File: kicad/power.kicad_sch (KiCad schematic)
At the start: 23 parts, among them Q1 AO3407A, Q4 AO3407A, SW2 SS-12F49-G050, U4 MP2322GQH-Z

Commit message: Updates to power
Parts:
- removed C46: 47uF, MyParts:C1206, symbol MyParts:GRM31CR61E476ME44L
- removed C47: 100nF, MyParts:C0603, symbol MyParts:CC0603KRX7R9BB104
- removed C48: 100nF, PCM_JLCPCB:C_0402, symbol PCM_JLCPCB-Capacitors:0402,100nF,(2)
- removed C49, C50: 10uF, PCM_JLCPCB:C_0805, symbol PCM_JLCPCB-Capacitors:0805,10uF,(2)
- removed C51: 100nF, PCM_JLCPCB:C_0603, symbol PCM_JLCPCB-Capacitors:0603,100nF
- removed C52: 22pF, PCM_JLCPCB:C_0603, symbol PCM_JLCPCB-Capacitors:0603,22pF
- removed C53: 22uF, PCM_JLCPCB:C_0805, symbol PCM_JLCPCB-Capacitors:0805,22uF
- removed C54: 1uF, PCM_JLCPCB:C_0402, symbol PCM_JLCPCB-Capacitors:0402,1uF
- removed DC1: DC-005-2.5A-2.0, MyParts:CONN-TH_DC-005-2.5A-2.0, symbol MyParts:DC-005-2.5A-2.0
- removed F1: 1812L110/48QR, MyParts:F1812, symbol MyParts:1812L110_48QR
- removed L11: 3.3uH, MyParts:IND-SMD_L3.0-W3.0-1, symbol MyParts:ANR3015T4R7M
- removed Q1, Q4: AO3407A, MyParts:SOT-23-3_L2.9-W1.6-P1.90-LS2.8-BR, symbol MyParts:AO3407A
- removed R20: 10kΩ, PCM_JLCPCB:R_0603, symbol PCM_JLCPCB-Resistors:0603,10kΩ
- removed R21: 976kΩ, Resistor_SMD:R_0805_2012Metric, symbol Device:R
- removed R22: 100kΩ, PCM_JLCPCB:R_0603, symbol PCM_JLCPCB-Resistors:0603,100kΩ
- removed R23: 220kΩ, PCM_JLCPCB:R_0603, symbol PCM_JLCPCB-Resistors:0603,220kΩ
- removed SW2: SS-12F49-G050, MyParts:SW-TH_SS-12F45-GXXX, symbol MyParts:SS-12F49-G050
- removed TP3: RH-5016, MyParts:TESTPOINT-SMD_L3.0-W2.0, symbol MyParts:RH-5016
- removed U4: MP2322GQH-Z, MyParts:QFN-8_L2.0-W1.5-P0.50-BL, symbol MyParts:MP2322GQH-Z
- added DC1: DC007B-2.5-J, MyParts:DC-IN-TH_HX-DC007B-2.5, symbol MyParts:DC007B-2.5-J
- added Q11, Q12: DMP3013SFV-7, MyParts:DFN-8_L3.3-W3.3-P0.65-BL, symbol MyParts:DMP3013SFV-7
- added R21: 10kΩ, PCM_JLCPCB:R_0603, symbol PCM_JLCPCB-Resistors:0603,10kΩ
- added SW4: SS-12F49-G050, MyParts:SW-TH_SS-12F45-GXXX, symbol MyParts:SS-12F49-G050
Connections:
- net 12V: now also Q12.5 (D)
- net 12V_IN: now also DC1.1, Q11.5 (D)
- net GND: now also DC1.2, DC1.3, Q11.4 (G), SW4.3
- new net: Q11.1 (S), Q11.2 (S), Q11.3 (S), Q12.1 (S), Q12.2 (S), Q12.3 (S), R21.1
- new net: R21.2, SW4.1
- new net: Q12.4 (G), SW4.2
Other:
- added sheet Power_3V3 (power_3v3.kicad_sch)
- added sheet Power_5V (power_5v.kicad_sch)
- note added: "12V DC input jack"
- note added: "12V in Out 5V and 3V3"
- note added: "2.5mm 20V 6.8mm 7A DC Power Jack Right Angle"
- note removed: "->"
- note removed: "0.1%"
- note removed: "1%"
- note removed: "1.1A Fuse 48VDC"
- note removed: "12V DC input fused to 1.1A max"
- note removed: "12V to 3V3 Buck"
- note removed: "12V_IN_FUSED is the input, 12V is the output (load)"
- note removed: "25V"
- note removed: "50V"
- note removed: "Circuit to convert 12V DC to 3V3 DC 12V is reverse polatiry and over voltage protected MP2322 used to convert 12V to 3V3 DC 12V DC out will draw max 600mA 3V3 DC out will draw max 400mA Buck modeled after John Teel's YouTube video: https://www.youtube.com/watch?v=rLHW4gU6idU and referencing the MP2322 datasheet"
- note removed: "From MP2322 Datasheet:"
- note removed: "Notes:"
- note removed: "Off"
- note removed: "On"
- note removed: "Q4 protects against reverse polarity. SW2 controls the gate of Q1, turning current on/off. The MOSFET is P-Channel."
- note removed: "gate"
- moved on the sheet: TP1

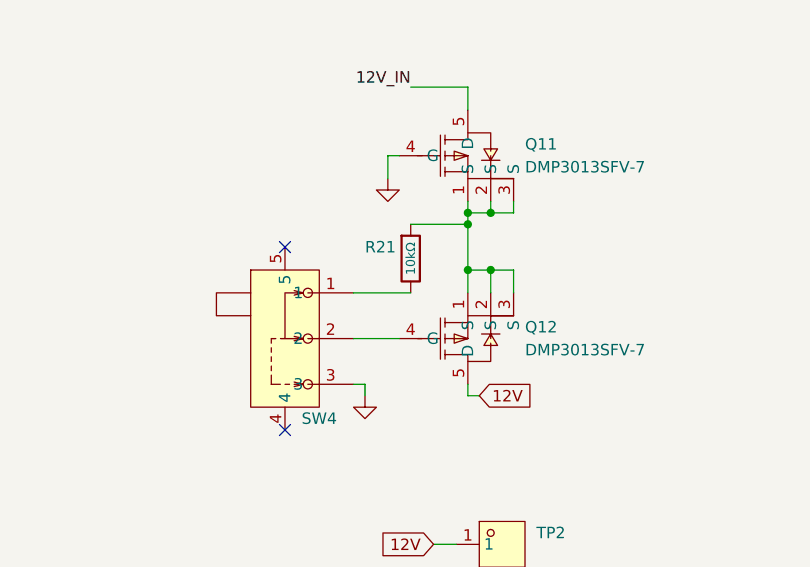
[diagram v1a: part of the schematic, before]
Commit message: Working on CM4 IO
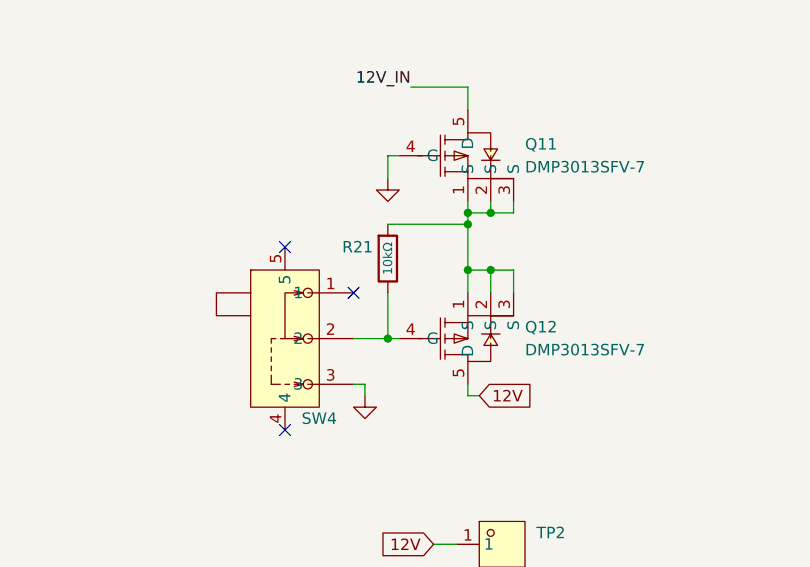
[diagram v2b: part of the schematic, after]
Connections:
- net at R21.2: now also Q12.4 (G), SW4.2; no longer SW4.1
- no-connect marks 2 -> 3
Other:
- moved on the sheet: R21
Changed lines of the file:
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@@
+	)
+	(junction
+		(at 161.29 49.53)
+		(diameter 0)
+		(color 0 0 0 0)
 	)
 	(junction
@@
 	)
 	(no_connect
+		(at 157.48 44.45)
+	)
+	(no_connect
 		(at 149.86 39.37)
 	)
@@
 	(wire
 		(pts
-			(xy 163.83 36.83) (xy 170.18 36.83)
-		)
-		(stroke
-			(width 0)
-			(type default)
-		)
-	)
-	(wire
-		(pts
 			(xy 170.18 24.13) (xy 170.18 21.59)
 		)
@@
 	(wire
 		(pts
+			(xy 161.29 44.45) (xy 161.29 49.53)
+		)
+		(stroke
+			(width 0)
+			(type default)
+		)
+	)
+	(wire
+		(pts
 			(xy 170.18 55.88) (xy 171.45 55.88)
 		)
@@
 	(wire
 		(pts
+			(xy 161.29 36.83) (xy 170.18 36.83)
+		)
+		(stroke
+			(width 0)
+			(type default)
+		)
+	)
+	(wire
+		(pts
 			(xy 170.18 41.91) (xy 170.18 44.45)
 		)
@@
 		(pts
 			(xy 91.44 41.91) (xy 92.71 41.91)
-		)
-		(stroke
-			(width 0)
-			(type default)
-		)
-	)
-	(wire
-		(pts
-			(xy 157.48 44.45) (xy 163.83 44.45)
 		)
 		(stroke
@@
 	(symbol
 		(lib_id "PCM_JLCPCB-Resistors:0603,10kΩ")
-		(at 163.83 40.64 0)
+		(at 161.29 40.64 0)
 		(unit 1)
 		(body_style 1)
@@
 		(dnp no)
 		(property "Reference" "R21"
-			(at 158.75 39.37 0)
+			(at 156.21 39.37 0)
 			(show_name no)
 			(do_not_autoplace no)
@@
 		)
 		(property "Value" "10kΩ"
-			(at 163.83 40.64 90)
+			(at 161.29 40.64 90)
 			(show_name no)
 			(do_not_autoplace yes)
@@
 		)
 		(property "Footprint" "PCM_JLCPCB:R_0603"
-			(at 162.052 40.64 90)
+			(at 159.512 40.64 90)
 			(hide yes)
 			(show_name no)
@@
 		)
 		(property "Datasheet" "https://www.lcsc.com/datasheet/lcsc_datasheet_2206010045_UNI-ROYAL-Uniroyal-Elec-0603WAF1002T5E_C25804.pdf"
-			(at 163.83 40.64 0)
+			(at 161.29 40.64 0)
 			(hide yes)
 			(show_name no)
@@
 		)
 		(property "Description" "100mW Thick Film Resistors 75V ±100ppm/°C ±1% 10kΩ 0603 Chip Resistor - Surface Mount ROHS"
-			(at 163.83 40.64 0)
+			(at 161.29 40.64 0)
 			(hide yes)
 			(show_name no)
@@
 		)
 		(property "LCSC" "C25804"
-			(at 163.83 40.64 0)
+			(at 161.29 40.64 0)
 			(hide yes)
 			(show_name no)
@@
 		)
 		(property "Stock" "51181774"
-			(at 163.83 40.64 0)
+			(at 161.29 40.64 0)
 			(hide yes)
 			(show_name no)
@@
 		)
 		(property "Price" "0.004USD"
-			(at 163.83 40.64 0)
+			(at 161.29 40.64 0)
 			(hide yes)
 			(show_name no)
@@
 		)
 		(property "Process" "SMT"
-			(at 163.83 40.64 0)
+			(at 161.29 40.64 0)
 			(hide yes)
 			(show_name no)
@@
 		)
 		(property "Minimum Qty" "20"
-			(at 163.83 40.64 0)
+			(at 161.29 40.64 0)
 			(hide yes)
 			(show_name no)
@@
 		)
 		(property "Attrition Qty" "10"
-			(at 163.83 40.64 0)
+			(at 161.29 40.64 0)
 			(hide yes)
 			(show_name no)
@@
 		)
 		(property "Class" "Basic Component"
-			(at 163.83 40.64 0)
+			(at 161.29 40.64 0)
 			(hide yes)
 			(show_name no)
@@
 		)
 		(property "Category" "Resistors,Chip Resistor - Surface Mount"
-			(at 163.83 40.64 0)
+			(at 161.29 40.64 0)
 			(hide yes)
 			(show_name no)
@@
 		)
 		(property "Manufacturer" "UNI-ROYAL(Uniroyal Elec)"
-			(at 163.83 40.64 0)
+			(at 161.29 40.64 0)
 			(hide yes)
 			(show_name no)
@@
 		)
 		(property "Part" "0603WAF1002T5E"
-			(at 163.83 40.64 0)
+			(at 161.29 40.64 0)
 			(hide yes)
 			(show_name no)
@@
 		)
 		(property "Resistance" "10kΩ"
-			(at 163.83 40.64 0)
+			(at 161.29 40.64 0)
 			(hide yes)
 			(show_name no)
@@
 		)
 		(property "Power(Watts)" "100mW"
-			(at 163.83 40.64 0)
+			(at 161.29 40.64 0)
 			(hide yes)
 			(show_name no)
@@
 		)
 		(property "Type" "Thick Film Resistors"
-			(at 163.83 40.64 0)
+			(at 161.29 40.64 0)
 			(hide yes)
 			(show_name no)
@@
 		)
 		(property "Overload Voltage (Max)" "75V"
-			(at 163.83 40.64 0)
+			(at 161.29 40.64 0)
 			(hide yes)
 			(show_name no)
@@
 		)
 		(property "Operating Temperature Range" "-55°C~+155°C"
-			(at 163.83 40.64 0)
+			(at 161.29 40.64 0)
 			(hide yes)
 			(show_name no)
@@
 		)
 		(property "Tolerance" "±1%"
-			(at 163.83 40.64 0)
+			(at 161.29 40.64 0)
 			(hide yes)
 			(show_name no)
@@
 		)
 		(property "Temperature Coefficient" "±100ppm/°C"
-			(at 163.83 40.64 0)
-			(hide yes)
-			(show_name no)
+			(at 161.29 40.64 0)
+			(hide yes)
+			(show_name no)

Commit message: Before adding CAN
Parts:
- renumbered Q11 to Q3, Q12 to Q4, R21 to R24, SW4 to SW2, TP1 to TP3, TP2 to TP4
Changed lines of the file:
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@@
 		(in_pos_files yes)
 		(dnp no)
-		(property "Reference" "R21"
+		(property "Reference" "R24"
 			(at 156.21 39.37 0)
 			(show_name no)
@@
 			(project "rcm_dish_controller"
 				(path "/10d7c3e5-be4d-4306-a59e-500b86bd141f/f4424325-c15a-4f12-b98c-68501db44bed"
-					(reference "R21")
+					(reference "R24")
 					(unit 1)
 				)
@@
 		(dnp no)
 		(fields_autoplaced yes)
-		(property "Reference" "Q11"
+		(property "Reference" "Q3"
 			(at 176.53 27.9399 0)
 			(show_name no)
@@
 			(project "rcm_dish_controller"
 				(path "/10d7c3e5-be4d-4306-a59e-500b86bd141f/f4424325-c15a-4f12-b98c-68501db44bed"
-					(reference "Q11")
+					(reference "Q3")
 					(unit 1)
 				)
@@
 		(dnp no)
 		(fields_autoplaced yes)
-		(property "Reference" "#PWR053"
+		(property "Reference" "#PWR027"
 			(at 161.29 38.1 0)
 			(hide yes)
@@
 			(project "rcm_dish_controller"
 				(path "/10d7c3e5-be4d-4306-a59e-500b86bd141f/f4424325-c15a-4f12-b98c-68501db44bed"
-					(reference "#PWR053")
+					(reference "#PWR027")
 					(unit 1)
 				)
@@
 		(dnp no)
 		(fields_autoplaced yes)
-		(property "Reference" "TP2"
+		(property "Reference" "TP4"
 			(at 177.8 71.1199 0)
 			(show_name no)
@@
 			(project "rcm_dish_controller"
 				(path "/10d7c3e5-be4d-4306-a59e-500b86bd141f/f4424325-c15a-4f12-b98c-68501db44bed"
-					(reference "TP2")
+					(reference "TP4")
 					(unit 1)
 				)
@@
 		(in_pos_files yes)
 		(dnp no)
-		(property "Reference" "SW4"
+		(property "Reference" "SW2"
 			(at 153.67 58.42 90)
 			(show_name no)
@@
 			(project "rcm_dish_controller"
 				(path "/10d7c3e5-be4d-4306-a59e-500b86bd141f/f4424325-c15a-4f12-b98c-68501db44bed"
-					(reference "SW4")
+					(reference "SW2")
 					(unit 1)
 				)
@@
 		(in_pos_files yes)
 		(dnp no)
-		(property "Reference" "Q12"
+		(property "Reference" "Q4"
 			(at 176.53 48.2599 0)
 			(show_name no)
@@
 			(project "rcm_dish_controller"
 				(path "/10d7c3e5-be4d-4306-a59e-500b86bd141f/f4424325-c15a-4f12-b98c-68501db44bed"
-					(reference "Q12")
+					(reference "Q4")
 					(unit 1)
 				)
@@
 		(dnp no)
 		(fields_autoplaced yes)
-		(property "Reference" "#PWR030"
+		(property "Reference" "#PWR028"
 			(at 92.71 49.53 0)
 			(hide yes)
@@
 			(project "rcm_dish_controller"
 				(path "/10d7c3e5-be4d-4306-a59e-500b86bd141f/f4424325-c15a-4f12-b98c-68501db44bed"
-					(reference "#PWR030")
+					(reference "#PWR028")
 					(unit 1)
 				)
@@
 		(dnp no)
 		(fields_autoplaced yes)
-		(property "Reference" "#PWR054"
+		(property "Reference" "#PWR029"
 			(at 158.75 62.23 0)
 			(hide yes)
@@
 			(project "rcm_dish_controller"
 				(path "/10d7c3e5-be4d-4306-a59e-500b86bd141f/f4424325-c15a-4f12-b98c-68501db44bed"
-					(reference "#PWR054")
+					(reference "#PWR029")
 					(unit 1)
 				)
@@
 		(dnp no)
 		(fields_autoplaced yes)
-		(property "Reference" "TP1"
+		(property "Reference" "TP3"
 			(at 95.25 52.0699 0)
 			(show_name no)
@@
 			(project "rcm_dish_controller"
 				(path "/10d7c3e5-be4d-4306-a59e-500b86bd141f/f4424325-c15a-4f12-b98c-68501db44bed"
-					(reference "TP1")
+					(reference "TP3")
 					(unit 1)
 				)

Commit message: More mods
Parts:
- added C20: 220uF, MyParts:CAP-SMD_BD6.3-L6.6-W6.6-FD, symbol MyParts:JVJ35V220M6X8
- added D35: SMAJ14A, PCM_JLCPCB:D_SMA, symbol PCM_JLCPCB-Diodes:TVS-Uni,SMAJ14A
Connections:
- net 12V: now also C20.1, D35.1
- net GND: now also C20.2, D35.2
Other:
- note added: "D35 clamps the 12V rail; place it physically at DC1. SMAJ14A clamps at 23.2V, under the +/-25V VGS of Q3/Q4 (gates at GND, so VGS follows the rail)."

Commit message: Add CAN JR45 - still working on it
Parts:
- renumbered D35 to D14, R24 to R22
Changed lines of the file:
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@@
 		(in_pos_files yes)
 		(dnp no)
-		(property "Reference" "R24"
+		(property "Reference" "R22"
 			(at 156.21 39.37 0)
 			(show_name no)
@@
 			(project "rcm_dish_controller"
 				(path "/10d7c3e5-be4d-4306-a59e-500b86bd141f/f4424325-c15a-4f12-b98c-68501db44bed"
-					(reference "R24")
+					(reference "R22")
 					(unit 1)
 				)
@@
 		(in_pos_files yes)
 		(dnp no)
-		(property "Reference" "D35"
+		(property "Reference" "D14"
 			(at 202.692 68.326 0)
 			(show_name no)
@@
 			(project "rcm_dish_controller"
 				(path "/10d7c3e5-be4d-4306-a59e-500b86bd141f/f4424325-c15a-4f12-b98c-68501db44bed"
-					(reference "D35")
+					(reference "D14")
 					(unit 1)
 				)
@@
 		(in_pos_files yes)
 		(dnp no)
-		(property "Reference" "#FLG06"
+		(property "Reference" "#FLG05"
 			(at 20.32 38.735 0)
 			(hide yes)
@@
 			(project "rcm_dish_controller"
 				(path "/10d7c3e5-be4d-4306-a59e-500b86bd141f/f4424325-c15a-4f12-b98c-68501db44bed"
-					(reference "#FLG06")
+					(reference "#FLG05")
 					(unit 1)
 				)
@@
 		(dnp no)
 		(fields_autoplaced yes)
-		(property "Reference" "#PWR027"
+		(property "Reference" "#PWR023"
 			(at 161.29 38.1 0)
 			(hide yes)
@@
 			(project "rcm_dish_controller"
 				(path "/10d7c3e5-be4d-4306-a59e-500b86bd141f/f4424325-c15a-4f12-b98c-68501db44bed"
-					(reference "#PWR027")
+					(reference "#PWR023")
 					(unit 1)
 				)
@@
 		(dnp no)
 		(fields_autoplaced yes)
-		(property "Reference" "#PWR028"
+		(property "Reference" "#PWR024"
 			(at 92.71 49.53 0)
 			(hide yes)
@@
 			(project "rcm_dish_controller"
 				(path "/10d7c3e5-be4d-4306-a59e-500b86bd141f/f4424325-c15a-4f12-b98c-68501db44bed"
-					(reference "#PWR028")
+					(reference "#PWR024")
 					(unit 1)
 				)
@@
 		(dnp no)
 		(fields_autoplaced yes)
-		(property "Reference" "#PWR029"
+		(property "Reference" "#PWR025"
 			(at 158.75 62.23 0)
 			(hide yes)
@@
 			(project "rcm_dish_controller"
 				(path "/10d7c3e5-be4d-4306-a59e-500b86bd141f/f4424325-c15a-4f12-b98c-68501db44bed"
-					(reference "#PWR029")
+					(reference "#PWR025")
 					(unit 1)
 				)
@@
 		(dnp no)
 		(fields_autoplaced yes)
-		(property "Reference" "#PWR0106"
+		(property "Reference" "#PWR026"
 			(at 185.42 83.82 0)
 			(hide yes)
@@
 			(project "rcm_dish_controller"
 				(path "/10d7c3e5-be4d-4306-a59e-500b86bd141f/f4424325-c15a-4f12-b98c-68501db44bed"
-					(reference "#PWR0106")
+					(reference "#PWR026")
 					(unit 1)
 				)
